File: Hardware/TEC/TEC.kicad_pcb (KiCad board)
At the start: 4 copper layers, 172 x 85 mm, 298 parts, among them J1 DEANS, J2 Data, J3 Conn_01x04, J4 Conn_01x04, J5 Conn_01x04, J6 Conn_01x04, Q1 2N7002PW, Q10 Si7141DP, Q11 Si7141DP, Q12 2N7002PW, Q13 2N7002PW, Q14 2N7002PW, Q15 2N7002PW, Q16 SQJ504EP, Q17 SQJ504EP, Q18 2N7002PW, Q19 2N7002PW, Q2 2N7002PW, Q20 2N7002PW, Q21 2N7002PW, Q22 SQJ504EP, Q23 SQJ504EP, Q24 2N7002PW, Q25 2N7002PW, Q26 2N7002PW, Q27 2N7002PW, Q28 SQJ504EP, Q29 SQJ504EP, Q3 2N7002PW, Q4 2N7002PW, Q5 2N7002PW, Q6 2N7002PW, Q7 SQJ504EP, Q8 SQJ504EP, Q9 2N7002PW, U1 LP3985-3.0, U10 LTC1923EUH, U11 LTC1693-1, U12 LTC1693-1, U13 LTC2053, U14 LTC1923EUH, U15 LTC1693-1, U16 LTC1693-1, U17 LTC2053, U18 LTC1923EUH, U19 LTC1693-1, U2 DAC108S085CISQ, U20 LTC1693-1, U3 ADC104S021, U4 LTC2053, U5 LTC1923EUH, U6 LTC1693-1, U7 LTC1693-1, U8 TPS7A26, U9 LTC2053

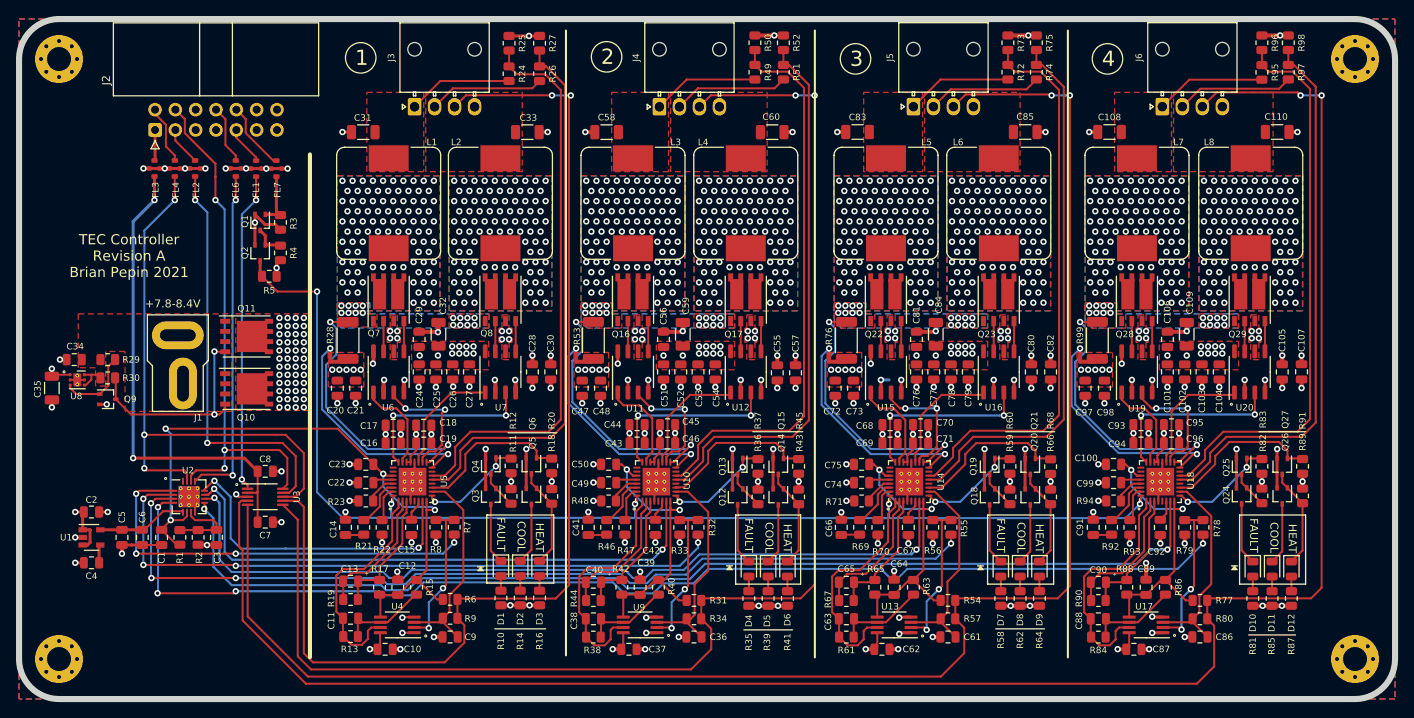
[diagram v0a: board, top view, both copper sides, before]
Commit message: Update to kicad 8
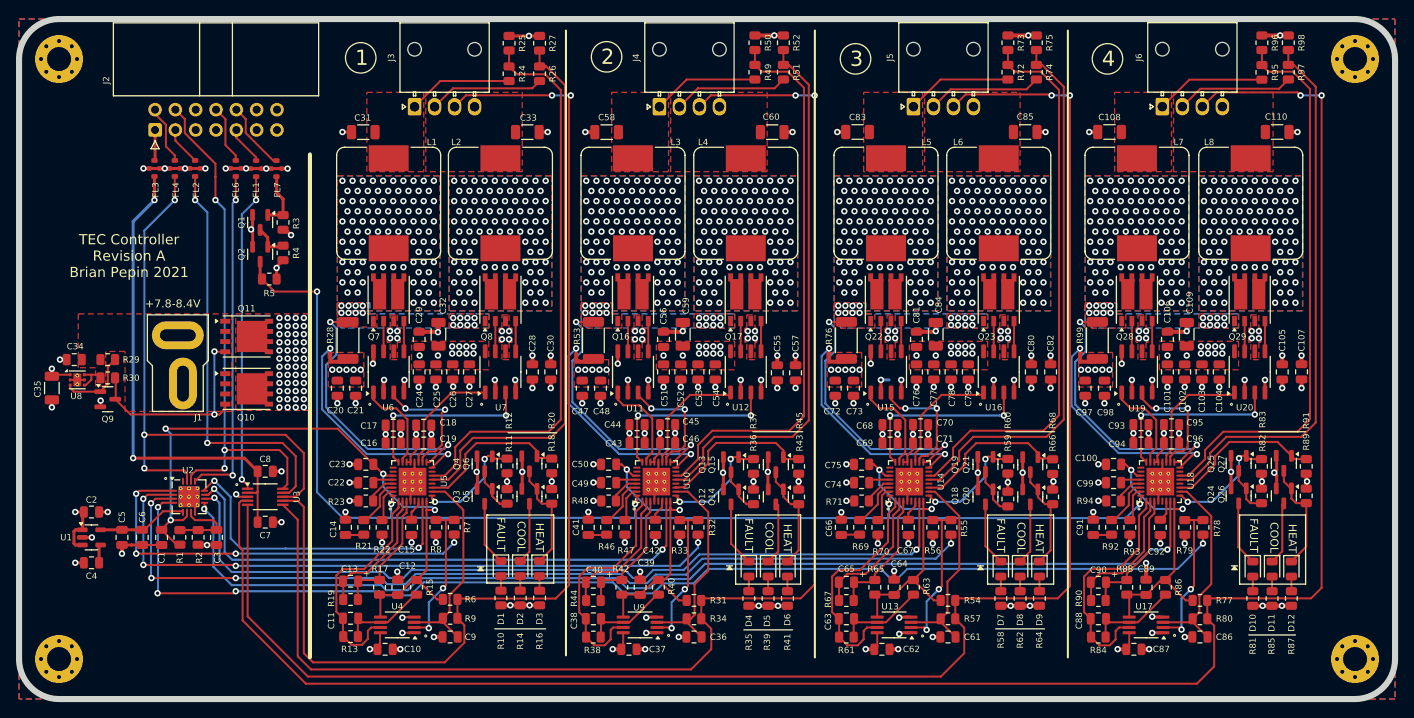
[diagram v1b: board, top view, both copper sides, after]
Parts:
- Q1, Q12, Q13, Q14, Q15, Q18, Q19, Q2, Q20, Q21, Q24, Q25, Q26, Q27, Q3, Q4, Q5, Q6, Q9: footprint Package_TO_SOT_SMD:SOT-323_SC-70 -> Package_TO_SOT_SMD:SOT-23
- moved Q13 0.86 mm to (139.0, 120.7)
- moved Q12 0.83 mm to (139.0, 124.7)
- moved Q4 0.81 mm to (108.2, 120.6)
- moved Q3 0.77 mm to (108.2, 124.7)
- moved Q19 0.58 mm to (170.8, 120.7)
- moved R36 0.57 mm to (141.8, 124.7)
- moved R37 0.57 mm to (141.8, 120.9)
- moved Q25 0.53 mm to (202.4, 120.5)
- moved Q18 0.52 mm to (170.8, 124.7)
- moved R11 0.51 mm to (111.0, 124.7)
- moved R12 0.51 mm to (111.0, 120.9)
- moved R89 0.46 mm to (210.9, 124.6)
- moved R91 0.46 mm to (210.9, 120.9)
- moved Q27 0.43 mm to (208.1, 120.5)
- moved Q15 0.38 mm to (144.6, 120.7)
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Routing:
- net GND: track 269.2 -> 260.2 mm, vias 160 -> 161
- net Net-(Q3-G): track 4.77 -> 6.84 mm
- net Net-(Q12-G): track 4.77 -> 6.23 mm
- net Net-(Q24-G): track 4.65 -> 6.03 mm
- net Net-(Q18-G): track 4.77 -> 6.08 mm
- net Net-(D3-K): track 12.6 -> 13.7 mm
- net Net-(D12-K): track 12.5 -> 13.6 mm
- net Net-(D9-K): track 12.5 -> 13.6 mm
- net Net-(D6-K): track 12.5 -> 13.5 mm
- net /sheet609C9431/~{FAULT}: track 13.5 -> 14.4 mm
- net +5V: track 91.4 -> 92.2 mm
- net /sheet609BE7FC/~{FAULT}: track 13.4 -> 13.9 mm
- net /LTC1923Channel/~{FAULT}: track 13.4 -> 13.9 mm
